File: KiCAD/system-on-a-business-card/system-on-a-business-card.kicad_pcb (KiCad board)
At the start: 2 copper layers, 85 x 55 mm, 105 parts, among them J1 USB_C_Receptacle, J2 X077-6428TSWCG01-H13, Q1 2N7002K, Q10 2N7002K, Q11 2N7002K, Q12 2N7002K, Q2 BSS84, Q3 2N7002K, Q4 2N7002K, Q5 2N7002K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

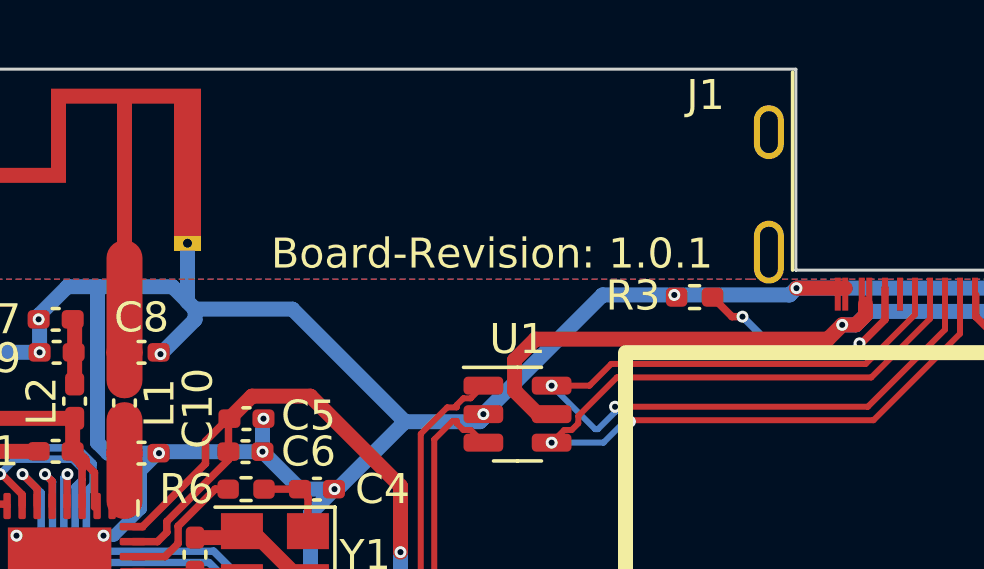
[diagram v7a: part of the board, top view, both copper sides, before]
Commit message: fixes #17: updates resistor values R53 and R54, updated board revision silkscreen
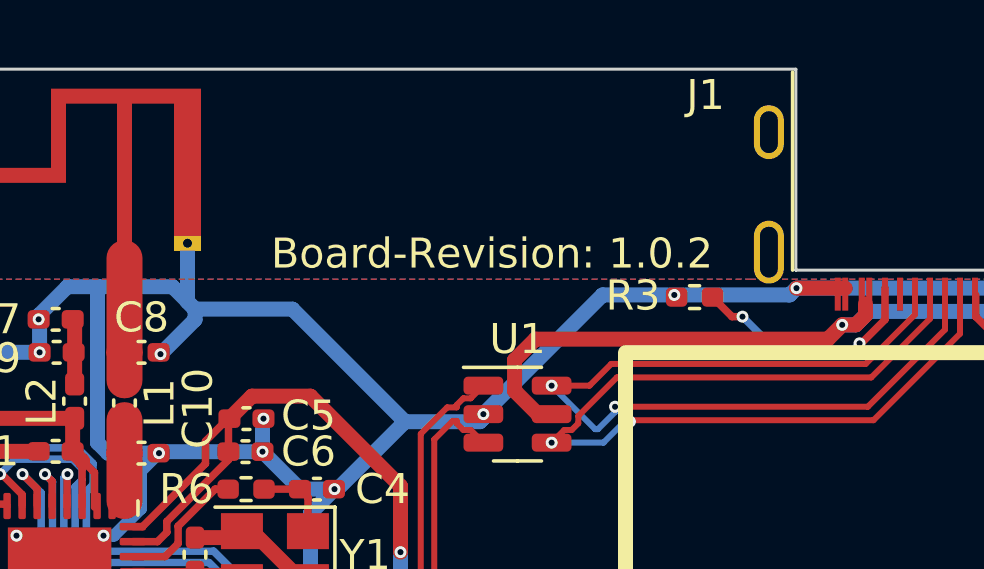
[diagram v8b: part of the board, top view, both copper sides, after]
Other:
- board text added: "Board-Revision: 1.0.2"
- board text removed: "Board-Revision: 1.0.1"
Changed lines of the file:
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@@
     (effects (font (size 1.5 1.5) (thickness 0.15)))
   )
-  (gr_text "Board-Revision: 1.0.1" (at 105.15 76.15) (layer "F.SilkS")
+  (gr_text "Board-Revision: 1.0.2" (at 105.15 76.15) (layer "F.SilkS")
     (effects (font (size 1 1) (thickness 0.15)))
   )
